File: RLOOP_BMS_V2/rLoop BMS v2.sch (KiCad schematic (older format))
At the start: 0 parts

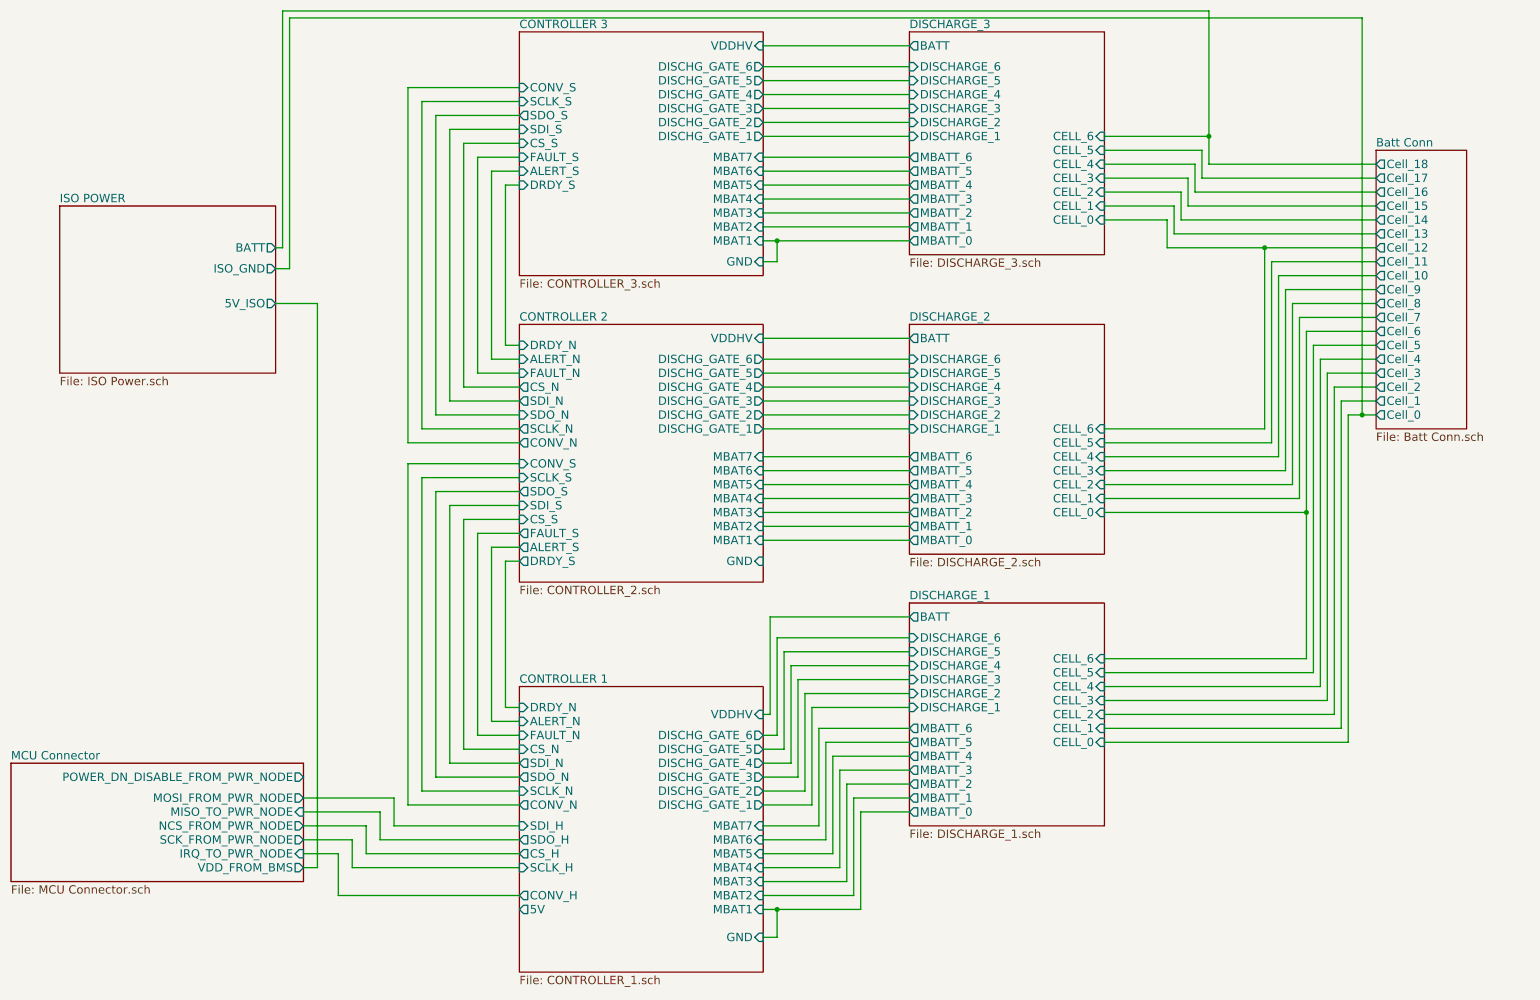
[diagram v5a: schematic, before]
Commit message: more WIP
making room for a thermal pad and power circuits
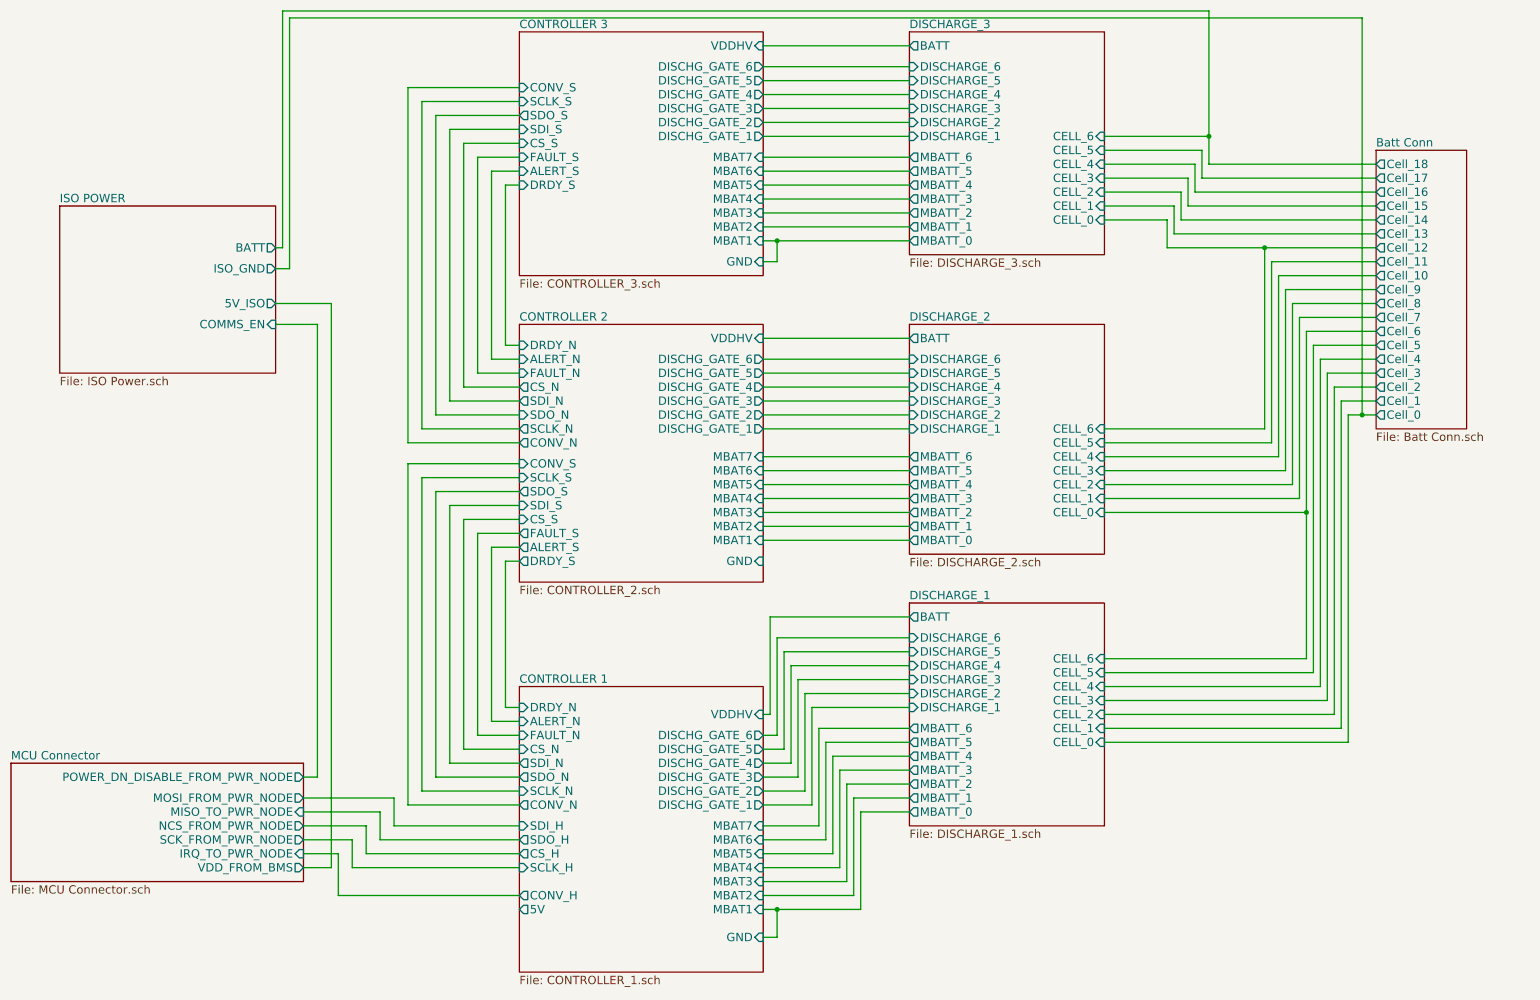
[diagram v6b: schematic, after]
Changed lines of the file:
@@
 Connection ~ 6100 7000
 Wire Wire Line
-	10400 3450 10200 3450
+	10200 3450 10400 3450
 Wire Wire Line
 	10200 3450 10200 5800
@@
 F3 "BATT" O R 2500 2250 60
 F4 "5V_ISO" O R 2500 2650 60
+F5 "COMMS_EN" I R 2500 2800 60
 $EndSheet
 Wire Wire Line
@@
 Connection ~ 10300 3450
 Wire Wire Line
-	2500 2650 2800 2650
-Wire Wire Line
-	2800 2650 2800 6700
-Wire Wire Line
-	2800 6700 2700 6700
+	2500 2650 2900 2650
+Wire Wire Line
+	2900 2650 2900 6700
+Wire Wire Line
+	2900 6700 2700 6700
+Wire Wire Line
+	2500 2800 2800 2800
+Wire Wire Line
+	2800 2800 2800 6050
+Wire Wire Line
+	2800 6050 2700 6050
 $EndSCHEMATC

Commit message: more WIP
TODO:
Fix pin 50
ground planes
figure out GND_2 weirdness
fix optoisolator 3d model
bq IC 3d model
triple check everything
BOM
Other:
- note added: "TODO ADD\nPIN 50 TO IC"
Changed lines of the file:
@@
 Wire Wire Line
 	2800 6050 2700 6050
+Wire Wire Line
+	6000 4500 6350 4500
+Wire Wire Line
+	6350 4500 6350 4350
+Connection ~ 6350 4350
+Text Notes 700  4250 0    197  ~ 0
+TODO ADD\nPIN 50 TO IC
 $EndSCHEMATC

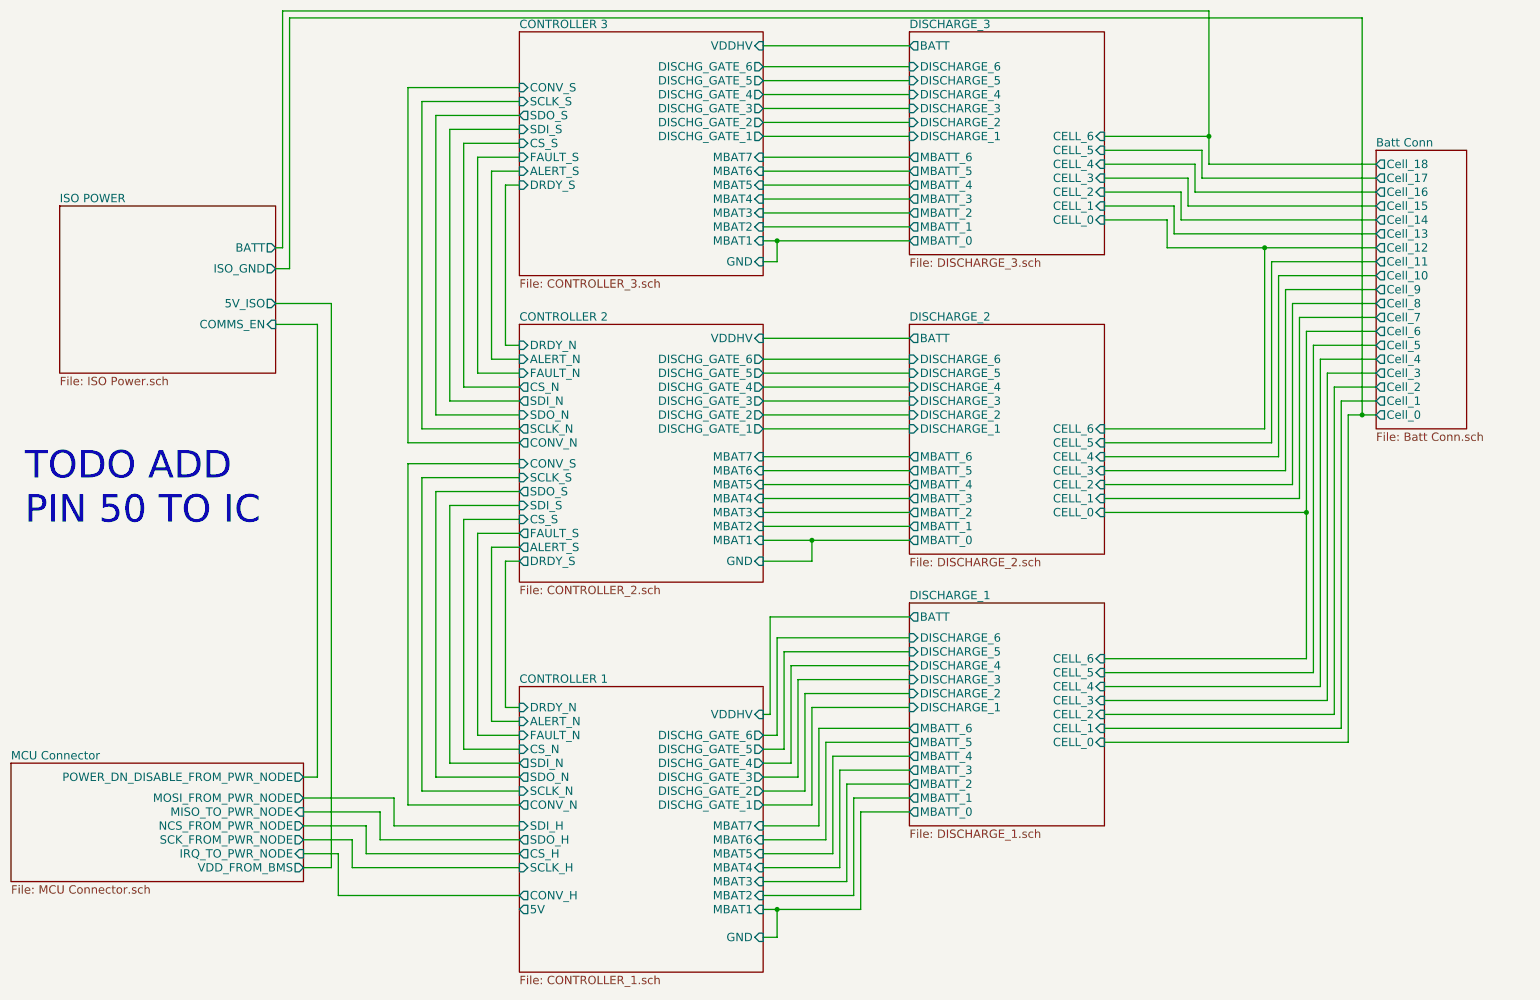
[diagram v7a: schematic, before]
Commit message: More WIP
Added connector for 1-Wire sensors if we want to put some sensors on the
heat-sinks. Just need to double check everything with the 3d-models.
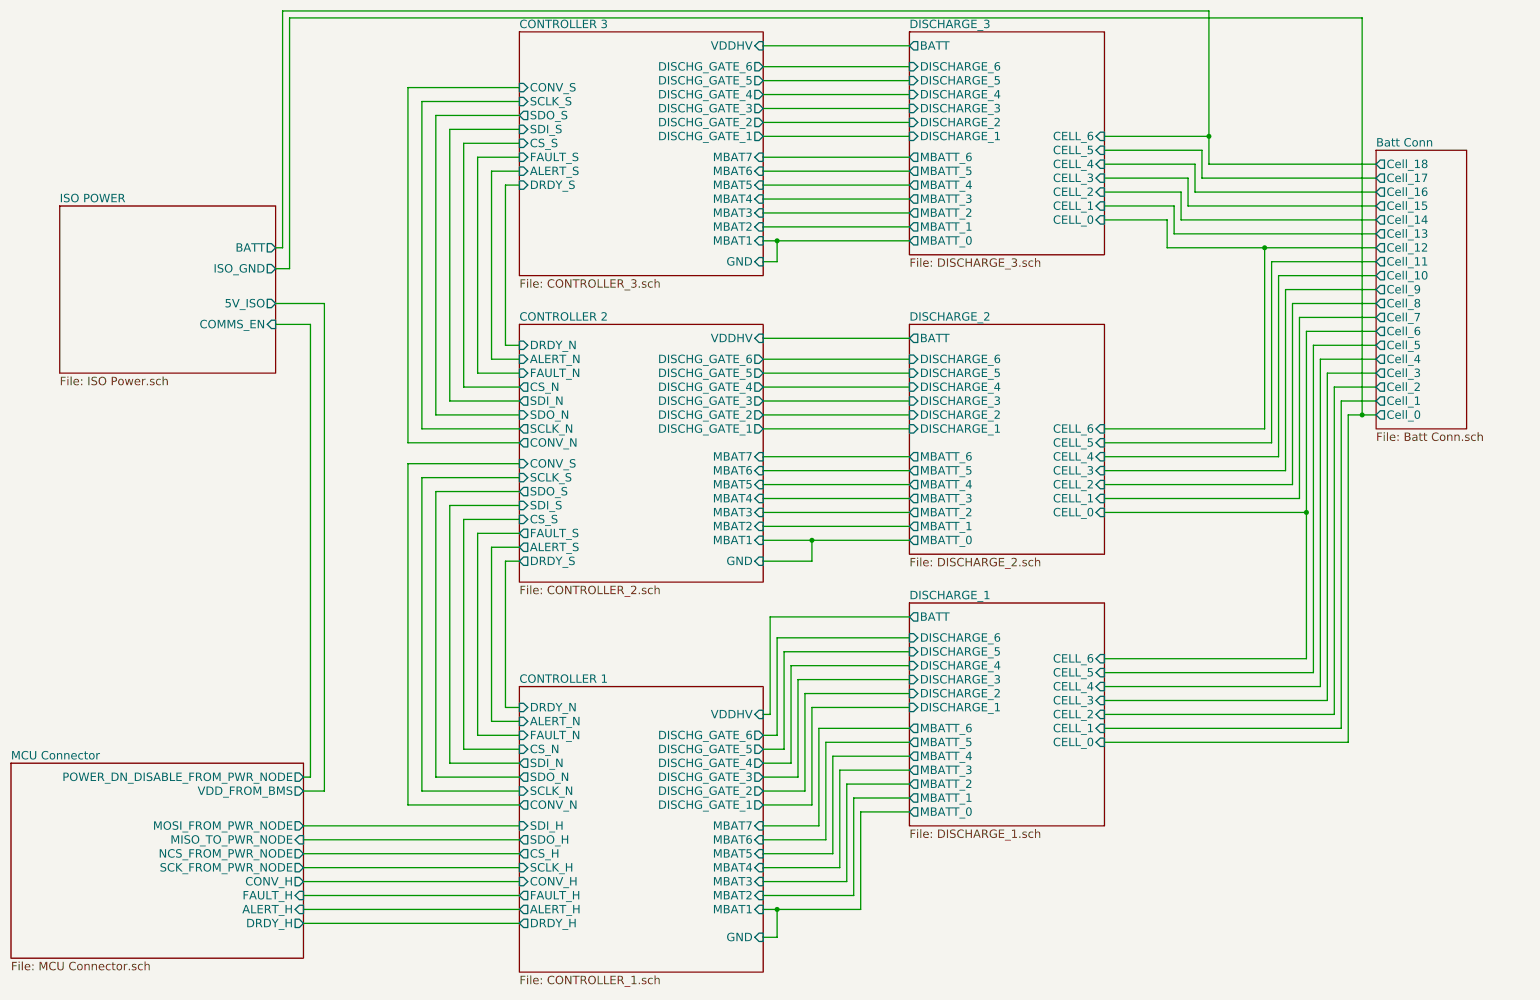
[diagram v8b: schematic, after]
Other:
- note removed: "TODO ADD\nPIN 50 TO IC"
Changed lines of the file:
@@
 EESchema Schematic File Version 2
+LIBS:rLoop BMS v2-rescue
 LIBS:power
 LIBS:device
@@
 $EndDescr
 $Sheet
-S 600  5950 2100 850
+S 600  5950 2100 1400
 U 590C18FD
 F0 "MCU Connector" 60
 F1 "MCU Connector.sch" 60
-F2 "IRQ_TO_PWR_NODE" I R 2700 6600 60
-F3 "MISO_TO_PWR_NODE" I R 2700 6300 60
-F4 "MOSI_FROM_PWR_NODE" O R 2700 6200 60
-F5 "SCK_FROM_PWR_NODE" O R 2700 6500 60
-F6 "NCS_FROM_PWR_NODE" O R 2700 6400 60
+F2 "CONV_H" O R 2700 6800 60
+F3 "MISO_TO_PWR_NODE" I R 2700 6500 60
+F4 "MOSI_FROM_PWR_NODE" O R 2700 6400 60
+F5 "SCK_FROM_PWR_NODE" O R 2700 6700 60
+F6 "NCS_FROM_PWR_NODE" O R 2700 6600 60
 F7 "POWER_DN_DISABLE_FROM_PWR_NODE" O R 2700 6050 60
-F8 "VDD_FROM_BMS" O R 2700 6700 60
+F8 "VDD_FROM_BMS" O R 2700 6150 60
+F9 "FAULT_H" I R 2700 6900 60
+F10 "ALERT_H" I R 2700 7000 60
+F11 "DRDY_H" O R 2700 7100 60
 $EndSheet
 $Sheet
@@
 	3450 6250 4250 6250
 Wire Wire Line
-	4250 6900 2950 6900
-Wire Wire Line
-	2950 6900 2950 6600
-Wire Wire Line
-	2950 6600 2700 6600
-Wire Wire Line
-	2700 6500 3050 6500
-Wire Wire Line
-	3050 6500 3050 6700
-Wire Wire Line
-	3050 6700 4250 6700
-Wire Wire Line
-	3150 6600 3150 6400
-Wire Wire Line
-	3150 6400 2700 6400
-Wire Wire Line
-	2700 6300 3250 6300
-Wire Wire Line
-	3250 6300 3250 6500
-Wire Wire Line
-	3250 6500 4250 6500
-Wire Wire Line
-	4250 6400 3350 6400
-Wire Wire Line
-	3350 6400 3350 6200
-Wire Wire Line
-	3350 6200 2700 6200
+	2700 6700 4250 6700
+Wire Wire Line
+	2700 6500 4250 6500
+Wire Wire Line
+	2700 6400 4250 6400
 $Sheet
 S 4250 700  1750 1750
@@
 F17 "SDI_H" I L 4250 6400 60
 F18 "SDO_H" O L 4250 6500 60
-F19 "CONV_H" O L 4250 6900 60
+F19 "CONV_H" I L 4250 6800 60
 F20 "SCLK_N" I L 4250 6150 60
 F21 "SDI_N" O L 4250 5950 60
 F22 "SDO_N" O L 4250 6050 60
 F23 "CONV_N" O L 4250 6250 60
-F24 "5V" O L 4250 7000 60
-F25 "VDDHV" I R 6000 5600 60
-F26 "GND" I R 6000 7200 60
-F27 "CS_H" O L 4250 6600 60
-F28 "FAULT_N" I L 4250 5750 60
-F29 "ALERT_N" I L 4250 5650 60
-F30 "DRDY_N" I L 4250 5550 60
+F24 "VDDHV" I R 6000 5600 60
+F25 "GND" I R 6000 7200 60
+F26 "CS_H" O L 4250 6600 60
+F27 "FAULT_N" I L 4250 5750 60
+F28 "ALERT_N" I L 4250 5650 60
+F29 "DRDY_N" I L 4250 5550 60
+F30 "FAULT_H" O L 4250 6900 60
+F31 "ALERT_H" O L 4250 7000 60
+F32 "DRDY_H" O L 4250 7100 60
 $EndSheet
 Wire Wire Line
@@
 	6000 4250 7050 4250
 Wire Wire Line
-	7050 4350 6000 4350
+	6000 4350 7050 4350
 Wire Wire Line
 	6000 5600 6050 5600
@@
 	9200 1450 8450 1450
 Wire Wire Line
-	3150 6600 4250 6600
+	2700 6600 4250 6600
 Wire Wire Line
 	4250 4200 3850 4200
@@
 Connection ~ 10300 3450
 Wire Wire Line
-	2500 2650 2900 2650
-Wire Wire Line
-	2900 2650 2900 6700
-Wire Wire Line
-	2900 6700 2700 6700
-Wire Wire Line
-	2500 2800 2800 2800
-Wire Wire Line
-	2800 2800 2800 6050
-Wire Wire Line
-	2800 6050 2700 6050
+	2500 2650 2850 2650
+Wire Wire Line
+	2850 2650 2850 6150
+Wire Wire Line
+	2850 6150 2700 6150
+Wire Wire Line
+	2500 2800 2750 2800
+Wire Wire Line
+	2750 2800 2750 6050
+Wire Wire Line
+	2750 6050 2700 6050
 Wire Wire Line
 	6000 4500 6350 4500
@@
 	6350 4500 6350 4350
 Connection ~ 6350 4350
-Text Notes 700  4250 0    197  ~ 0
-TODO ADD\nPIN 50 TO IC
+Wire Wire Line
+	2700 6800 4250 6800
+Wire Wire Line
+	2700 6900 4250 6900
+Wire Wire Line
+	4250 7000 2700 7000
+Wire Wire Line
+	2700 7100 4250 7100
 $EndSCHEMATC
